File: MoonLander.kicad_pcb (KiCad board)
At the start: 2 copper layers, 37.8 x 22.7 mm, 44 parts, among them IC1 MCP73831/2, IC2 BU33SD5, IC3 PRTR5V0U2X, IC4 CP2110-GM, IC5 LPC824M201JHI33, J1 Cortex_JTAG/SWD_10, P1 CONN_01X02, P2 CONN_01X02, P3 USB_OTG, P4 CONN_02X08, SW1 SW_PUSH, SW2 SW_PUSH, Y1 Crystal

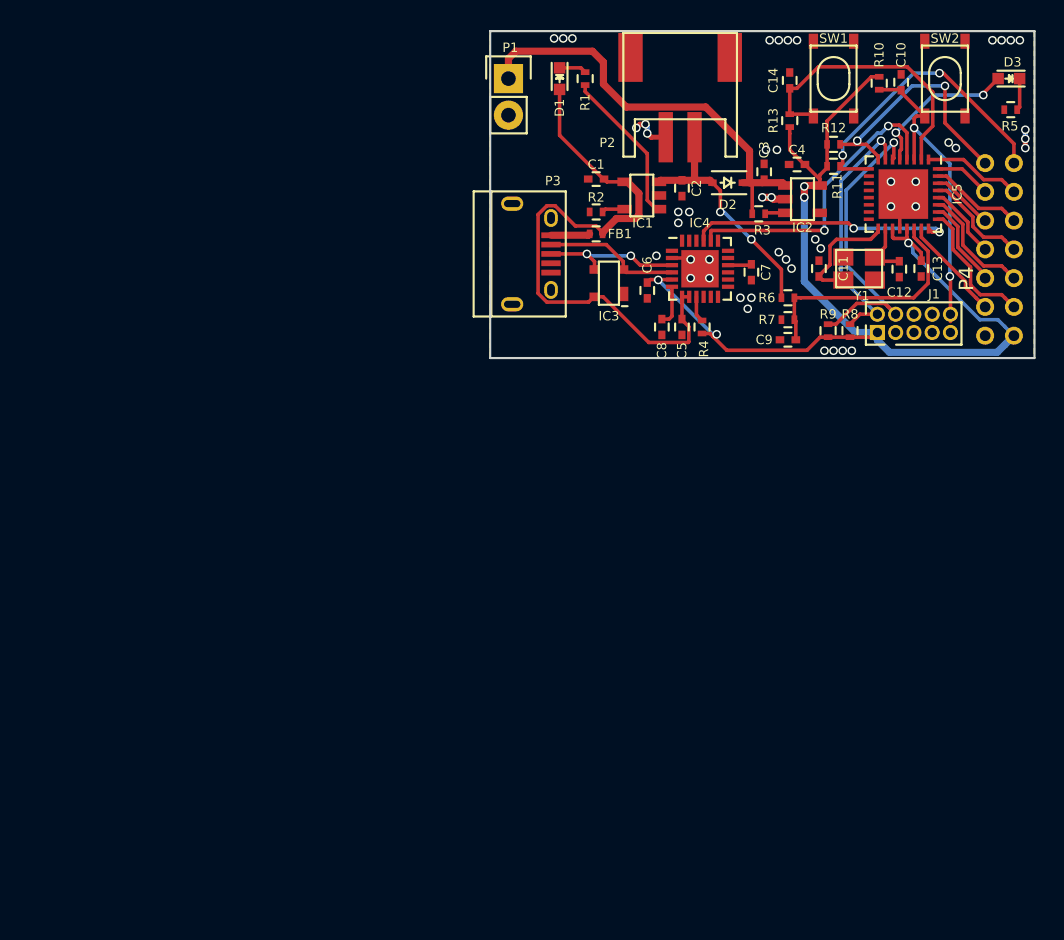
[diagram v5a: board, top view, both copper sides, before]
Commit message: need to squeeze on some mounting holes...
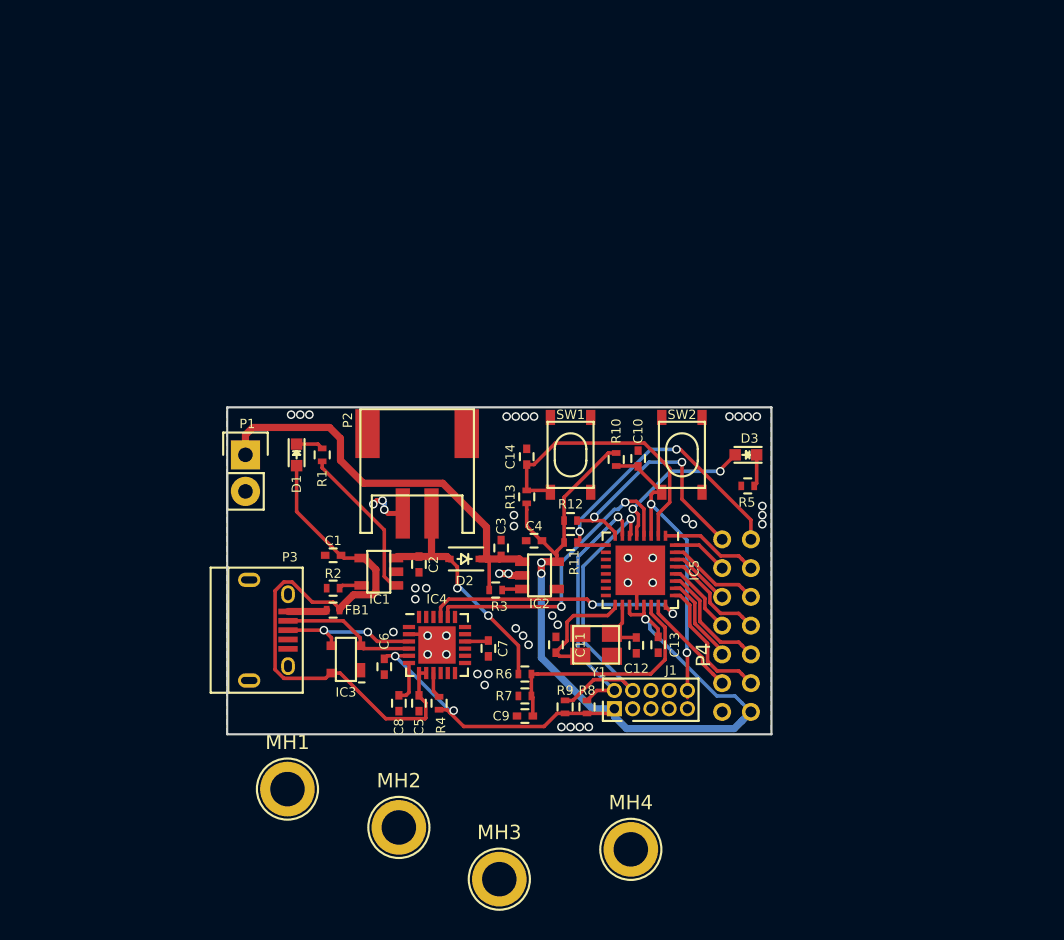
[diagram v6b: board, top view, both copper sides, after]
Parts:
- added MH1: MountingHole, GrayCatLabs:MH-M2, F.Cu at (133.5, 113.3)
- added MH2: MountingHole, GrayCatLabs:MH-M2, F.Cu at (141.2, 116.0)
- added MH3: MountingHole, GrayCatLabs:MH-M2, F.Cu at (148.2, 119.5)
- added MH4: MountingHole, GrayCatLabs:MH-M2, F.Cu at (157.4, 117.5)
- moved C1 31.9 mm to (136.7, 97.0)
- moved C11 31.9 mm to (152.1, 103.3)
- moved C6 31.9 mm to (140.2, 104.8)
- moved D1 31.9 mm to (134.1, 90.0)
- moved IC1 31.9 mm to (139.8, 98.2)
- moved P3 31.9 mm to (132.0, 102.2)
- moved P4 31.9 mm to (165.7, 107.9)
- moved R1 31.9 mm to (135.9, 90.0)
- moved R10 31.9 mm to (156.3, 90.4)
- moved R6 31.9 mm to (150.0, 105.3)
- moved R7 31.9 mm to (150.0, 106.8)
- moved Y1 31.9 mm to (154.9, 103.3)
- moved C10 31.9 mm to (157.9, 90.3)
- moved C7 31.9 mm to (147.4, 103.5)
- moved C8 31.9 mm to (141.2, 107.3)
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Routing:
- net (no net): track 14.7 -> 5.03 mm, vias 0 -> 34
- net /CPU/ISP_TXD: track 21.3 -> 30.9 mm
- net GND: track 8.94 -> 7.60 mm, vias 47 -> 13
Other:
- rule trace_min: 0.1524 -> 0.006
- rule via_min_size: 0.4 -> 0.015748

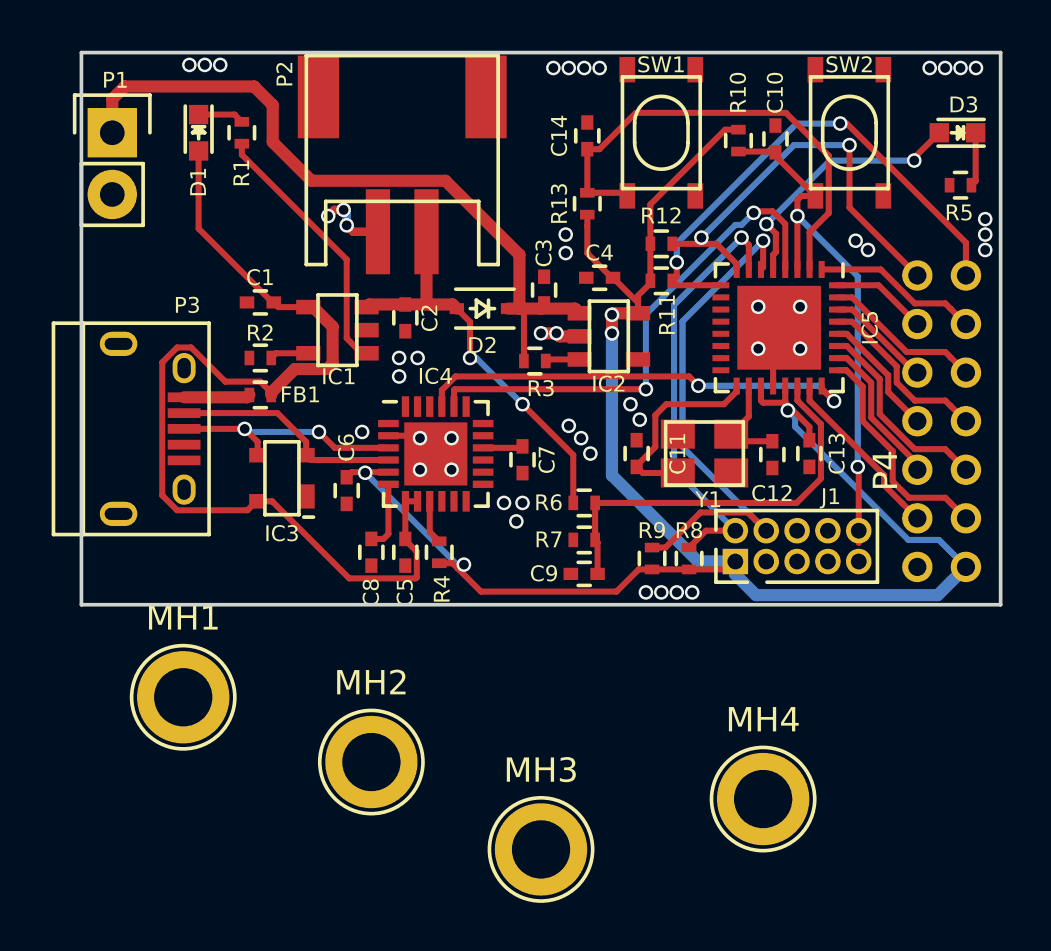
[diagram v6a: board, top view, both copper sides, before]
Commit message: made room for two M2 mounting holes
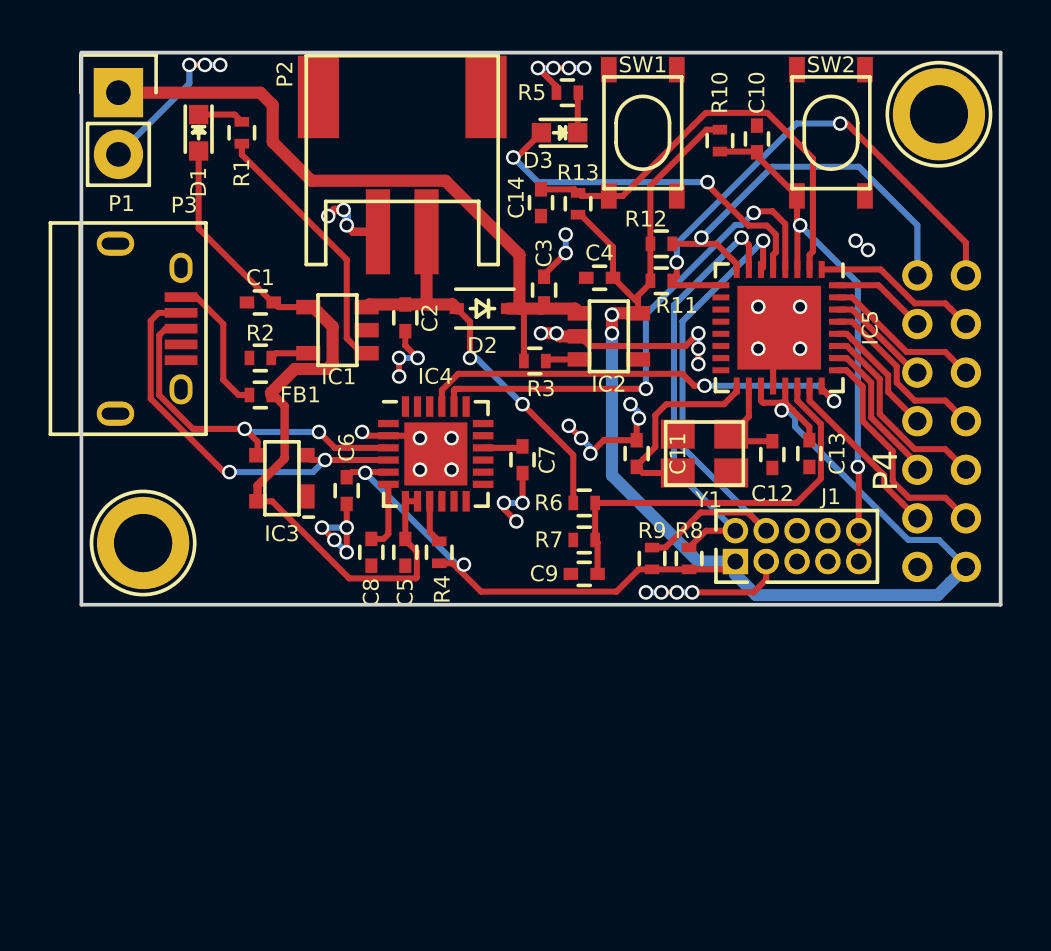
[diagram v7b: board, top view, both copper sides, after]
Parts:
- removed MH3, MH4: MountingHole, GrayCatLabs:MH-M2
- moved MH2 35.5 mm to (164.6, 89.3)
- moved R5 16.6 mm to (149.3, 88.4)
- moved D3 16.4 mm to (149.0, 90.0)
- moved MH1 6.56 mm to (131.8, 106.9)
- moved P3 4.13 mm to (131.8, 98.1)
- moved C14 3.35 mm to (148.2, 92.9), turned to 270 degrees
- moved P1 1.67 mm to (130.8, 88.4)
- moved C10 0.76 mm to (157.1, 90.3)
- moved R10 0.76 mm to (155.6, 90.4)
- moved SW1 0.76 mm to (152.4, 90.0)
- moved SW2 0.76 mm to (160.1, 90.0)
- moved R13 0.38 mm to (149.7, 93.0)
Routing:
- net GND: track 7.60 -> 48.2 mm, vias 13 -> 45
- net 5V_USB: track 42.1 -> 32.0 mm
- net /USB-Serial/USB_D-: track 9.53 -> 16.7 mm, vias 0 -> 2
- net /USB-Serial/USB_D+: track 10.0 -> 15.1 mm
- net /CPU/LED: track 10.8 -> 15.3 mm
- net Net-(FB1-Pad2): track 2.73 -> 5.83 mm
- net /PowerSupply/V_EXT: track 29.9 -> 27.9 mm
- net /CPU/ISP_ENTRY: track 19.8 -> 18.1 mm
- net /CPU/I2C0_SDA: track 17.7 -> 16.7 mm, vias 2 -> 1
- net /CPU/RESET: track 22.2 -> 21.2 mm
- net Net-(D3-Pad1): track 2.23 -> 1.66 mm
- net (no net): vias 34 -> 2

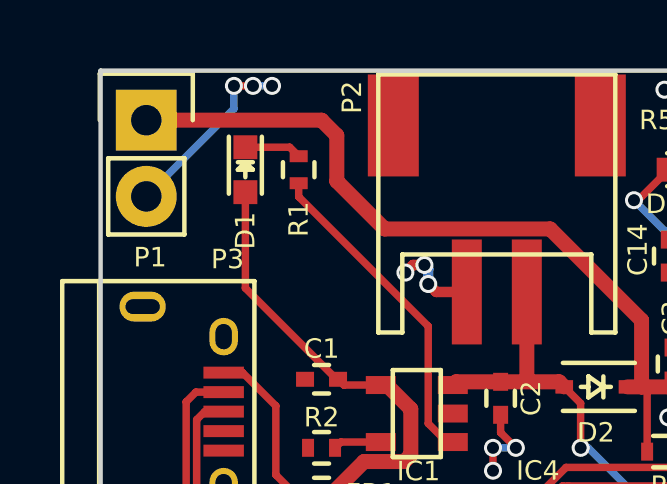
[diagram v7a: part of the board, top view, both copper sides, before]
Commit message: added some dimensions
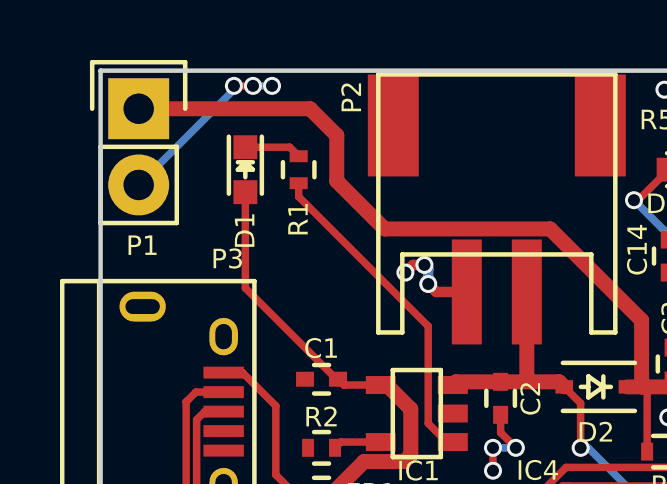
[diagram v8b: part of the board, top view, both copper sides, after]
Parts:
- moved P1 0.46 mm to (130.6, 88.0)
